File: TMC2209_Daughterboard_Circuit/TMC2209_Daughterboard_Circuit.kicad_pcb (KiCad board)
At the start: 2 copper layers, 4 parts, among them J6 Conn_01x04_Socket

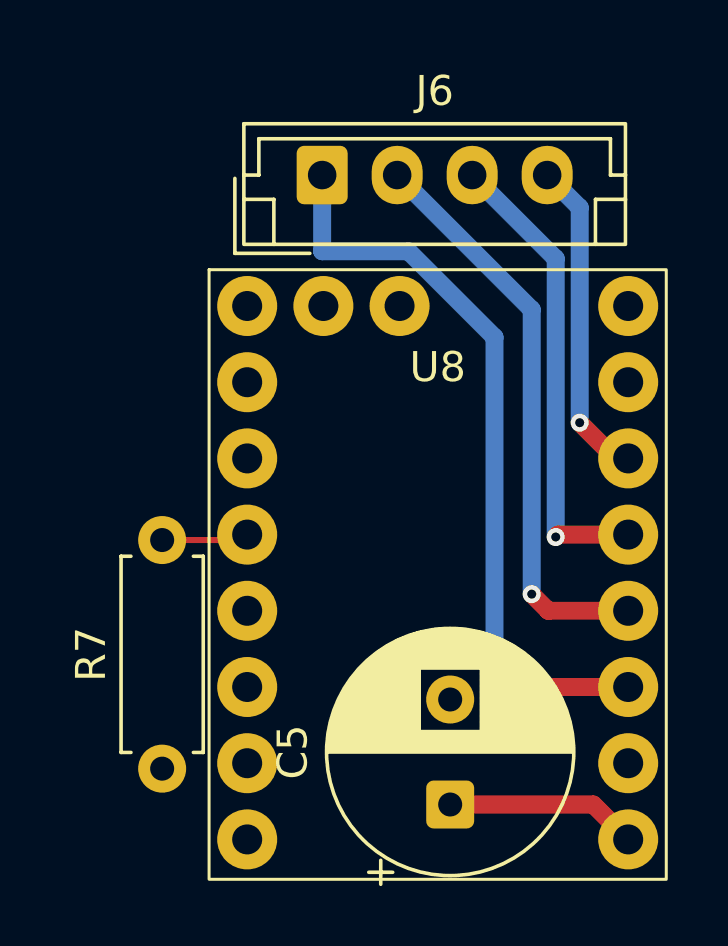
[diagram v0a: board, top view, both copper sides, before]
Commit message: Swap J4 to 2x06 header, drop KY-023 joysticks, rework TMC2209 daughterboard layout; add V0.2.0/V0.2.1 fab outputs
- PNP: J4 Conn_01x06 -> Conn_02x06 (PinHeader_2x06), removed Left/Right Joystick (U6/U10) from schematic and PCB, PCB re-routed (370 -> 366 segments area, vias 70 -> 58, zones 2 -> 1), ESP32-S3-DevKitC and MP1584EN footprints moved to Footprints lib, mask-to-copper clearance 0.005 mm
- TMC2209 daughterboard: PCB re-annotated/re-laid out (C5->C2, J6->J2, U8->U4, R7 removed)
- production/: PNP_V0.2.0 and V0.2.1 JLCPCB zips, BOM/CPL, netlist.ipc; fabrication-toolkit options
- code/: PlatformIO .gitignore and VS Code extension recommendations
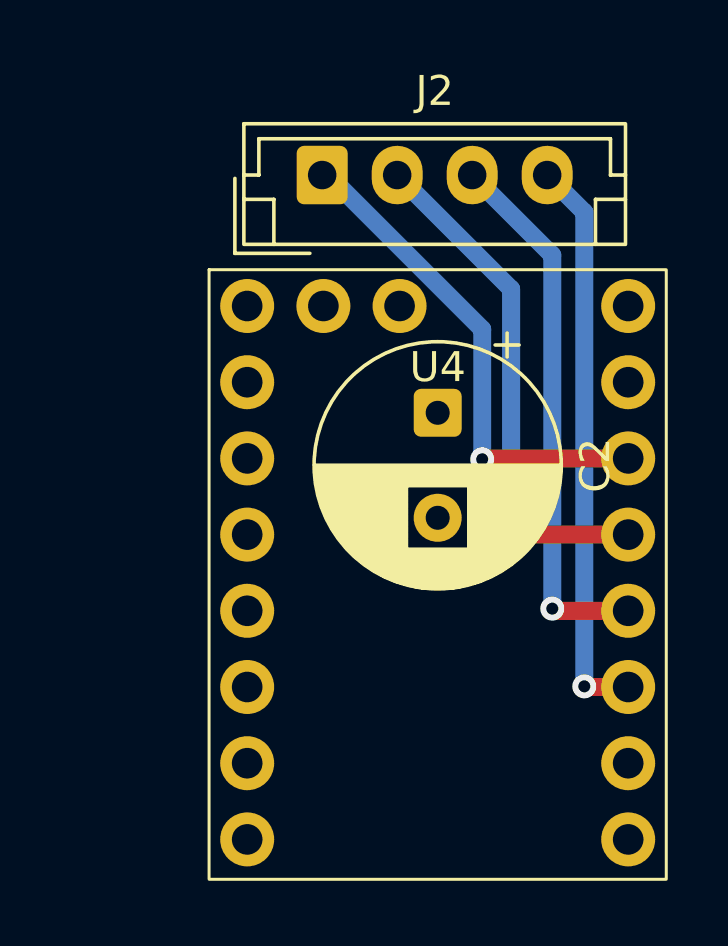
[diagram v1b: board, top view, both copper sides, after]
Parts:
- removed R7: 1K, Resistor_THT:R_Axial_DIN0207_L6.3mm_D2.5mm_P7.62mm_Horizontal
- moved C2 13.1 mm to (62.3, 40.3), turned to -90 degrees
- renumbered C5 to C2, J6 to J2, U8 to U4
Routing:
- net /A2: track 25.3 -> 16.7 mm
- net /B2: track 10.8 -> 19.0 mm
- net /B1: track 15.7 -> 18.1 mm
- net /RX: track 2.91 -> 0.51 mm
- net /A1: track 19.3 -> 17.4 mm
- net +24V: track 6.41 -> 7.82 mm
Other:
- copper layers 2 -> 4
